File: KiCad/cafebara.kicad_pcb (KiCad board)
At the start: 4 copper layers, 50 x 26.8 mm, 31 parts, among them J1 Micro_SD_Card_Det2, J2 USB_C_Receptacle_USB2.0_14P, J3 PROG, J4 505278-1933, J5 I2C, Q1 NMOS, SW1 SW_Push, U3 ATtiny1616-M

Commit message: Minor misc updates
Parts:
- added TP6: HPD, TestPoint:TestPoint_Pad_D1.5mm, F.Cu at (87.5, 60.8)
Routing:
- net HPD: track 41.9 -> 56.7 mm, vias 2 -> 3
- net +3.3V: track 7.29 -> 0.00 mm

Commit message: Misc changes to cafebara, add temperature board
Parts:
- J4: value 505278-1933 -> Conn_01x19_MountingPin; moved to F.Cu
- moved J4 6.02 mm to (78.2, 70.5), turned to 0 degrees
- moved J1 0.50 mm to (93.8, 47.5)
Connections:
- J4 pad 1: TMDS2+ -> HPD
- J4 pad 11: GND -> TMDS0-
- J4 pad 12: TMDSClk- -> GND
- J4 pad 13: unconnected-(J4-Pad13) -> TMDS0+
- J4 pad 14: unconnected-(J4-Pad14) -> TMDS1-
- J4 pad 15: /HDMI_SCL -> GND
- J4 pad 16: /HDMI_SDA -> TMDS1+
- J4 pad 17: GND -> TMDS2-
- J4 pad 18: +5V -> GND
- J4 pad 19: HPD -> TMDS2+
- J4 pad 2: GND -> +5V
- J4 pad 3: TMDS2- -> GND
- J4 pad 4: TMDS1+ -> /HDMI_SDA
- J4 pad 5: GND -> /HDMI_SCL
- J4 pad 6: TMDS1- -> unconnected-(J4-Pin_6-Pad6)
- J4 pad 7: TMDS0+ -> unconnected-(J4-Pin_7-Pad7)
- J4 pad 8: GND -> TMDSClk-
- J4 pad 9: TMDS0- -> GND
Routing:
- net HPD: track 56.7 -> 62.4 mm
- net TMDSClk-: track 3.88 -> 3.14 mm, vias 1 -> 0
- net TMDS2+: track 3.79 -> 3.07 mm, vias 1 -> 0
- net TMDS0-: track 3.76 -> 3.13 mm, vias 1 -> 0
- net TMDS1-: track 3.64 -> 3.11 mm, vias 1 -> 0
- net SD_VCC: track 21.0 -> 21.5 mm
- net SD_DECT: track 14.4 -> 14.9 mm
- net SD_D3: track 14.0 -> 14.5 mm
- net SD_D2: track 14.3 -> 14.8 mm
- net SD_D1: track 21.4 -> 21.9 mm
- net SD_D0: track 17.3 -> 17.8 mm
- net SD_CMD: track 14.0 -> 14.5 mm
- net SD_CLK: track 14.2 -> 14.7 mm
- net TMDSClk+: track 3.61 -> 3.11 mm, vias 1 -> 0
- net TMDS0+: track 3.48 -> 3.06 mm, vias 1 -> 0
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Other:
- board size 50 x 26.8 mm -> 50 x 32 mm

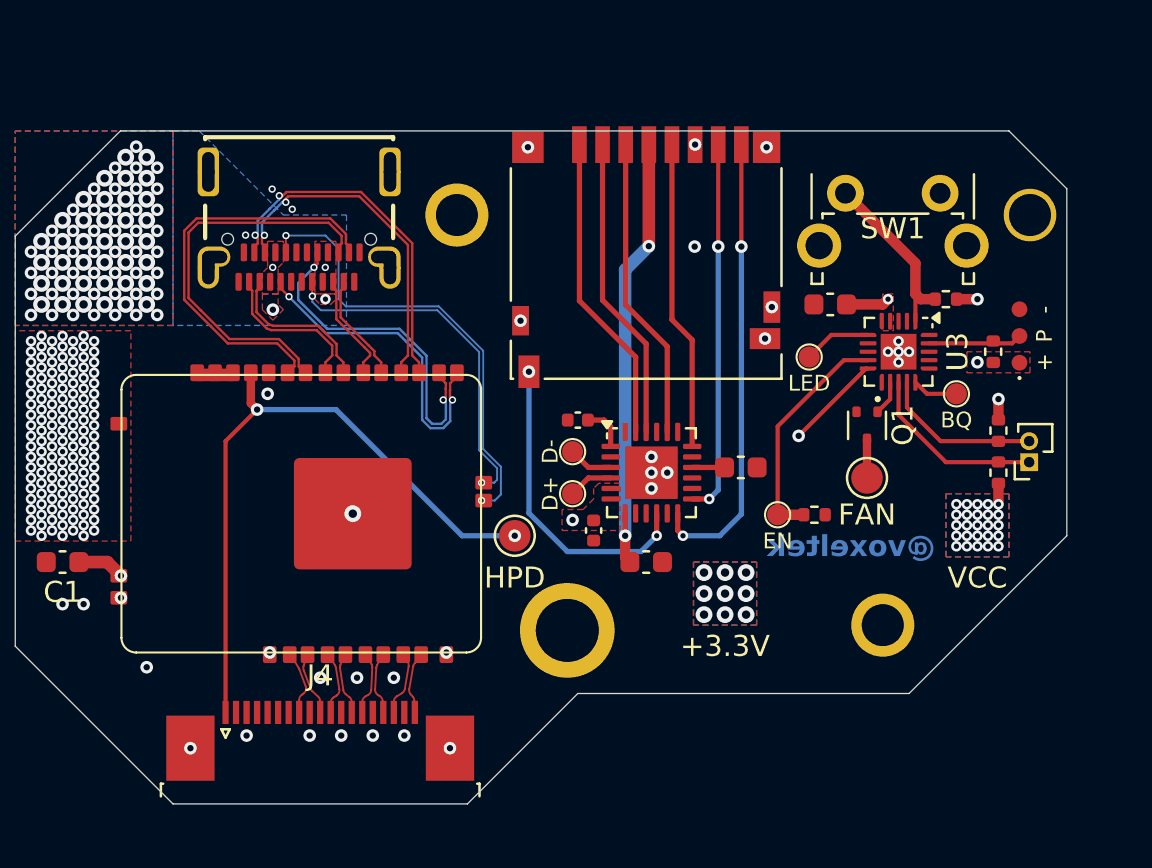
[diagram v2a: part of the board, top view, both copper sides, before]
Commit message: Add alert pin, EDID EEPROM, misc other changes
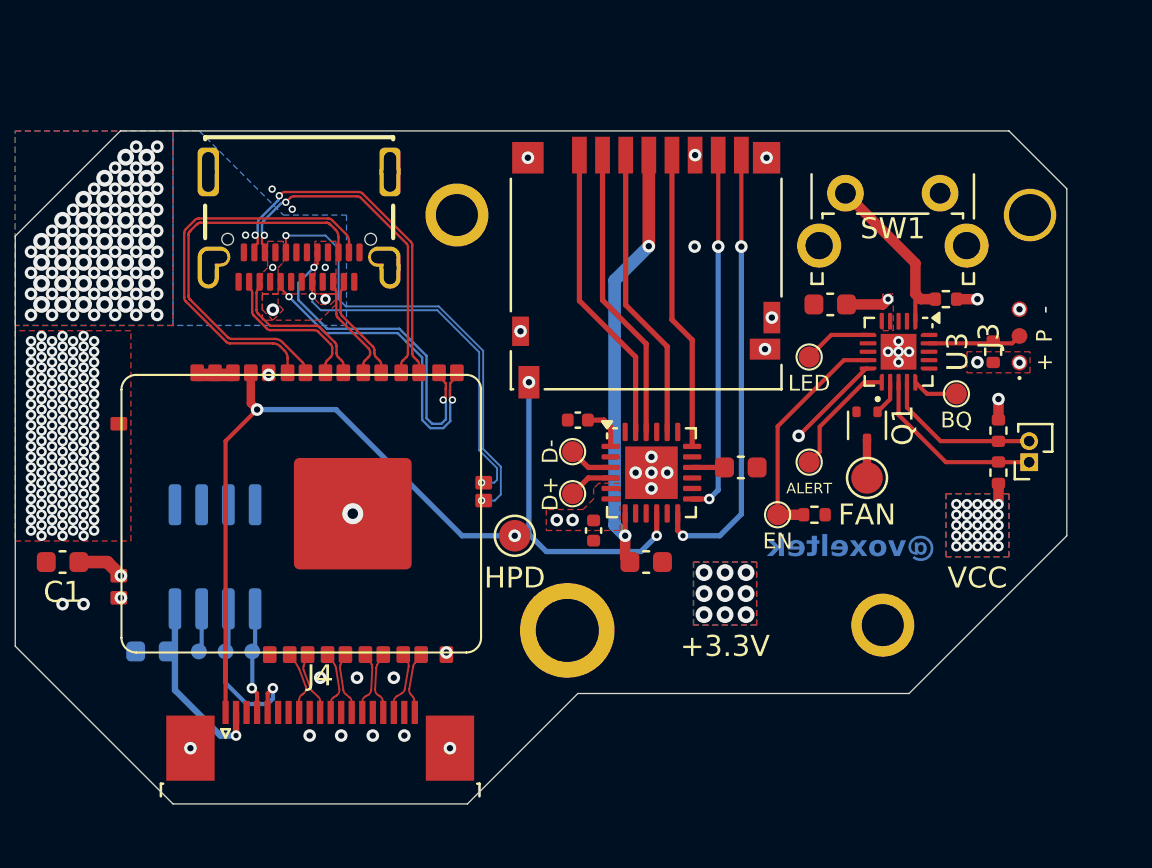
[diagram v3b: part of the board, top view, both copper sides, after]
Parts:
- added C7: 10uF, Capacitor_SMD:C_0603_1608Metric, B.Cu at (70.2, 66.2)
- added J6: EDID, cafebara:UPDI Pads, B.Cu at (73.8, 66.2)
- added TP7: ALERT, cafebara:TestPoint_Pad_D1.0mm_Small, F.Cu at (101.5, 57.2)
- added U4: M24C02-WMN, Package_SO:SOIC-8_3.9x4.9mm_P1.27mm, B.Cu at (73.2, 61.8)
- J3: footprint Stormbreaker:UPDI Pads -> cafebara:UPDI Pads
- moved J1 0.50 mm to (93.8, 48.0)
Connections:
- U3 pad 11: unconnected-(U3-PB3-Pad11) -> ~{ALERT}
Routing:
- net +5V: track 0.00 -> 8.77 mm, vias 0 -> 1
- net /HDMI_SCL: track 0.00 -> 8.10 mm, vias 0 -> 1
- net ~{ALERT}: track 0.00 -> 5.72 mm
- net /HDMI_SDA: track 0.00 -> 5.09 mm, vias 0 -> 1
- net /EEPROM_~{WC}: track 0.00 -> 2.08 mm
- net SD_D3: track 14.5 -> 14.0 mm
- net SD_D2: track 14.8 -> 14.3 mm
- net SD_D1: track 21.9 -> 21.4 mm
- net SD_D0: track 17.8 -> 17.3 mm
- net SD_CMD: track 14.5 -> 14.0 mm
- net SD_CLK: track 14.7 -> 14.2 mm
- net VCC: vias 29 -> 30
- net VBUS: vias 90 -> 91
- net GND: vias 173 -> 172
- net +3.3V: vias 10 -> 11

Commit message: Possibly planning to enlarge board...
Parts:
- removed the REF** at (112.0, 45.5)
- removed the REF** at (90.0, 65.2)
- removed the REF** at (105.0, 65.0)
- added H1: GND, TestPoint:TestPoint_Plated_Hole_D2.0mm, F.Cu at (105.0, 65.2)
- added H2: GND, TestPoint:TestPoint_Plated_Hole_D2.0mm, F.Cu at (112.0, 45.5)
- added H3: GND, TestPoint:TestPoint_Plated_Hole_D2.0mm, F.Cu at (90.0, 65.2)
- added H4: GND, TestPoint:TestPoint_Plated_Hole_D2.0mm, F.Cu at (66.5, 65.2)
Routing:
- net VBUS: vias 91 -> 60
- net GND: vias 172 -> 173
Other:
- outline, holes or cut-outs redrawn

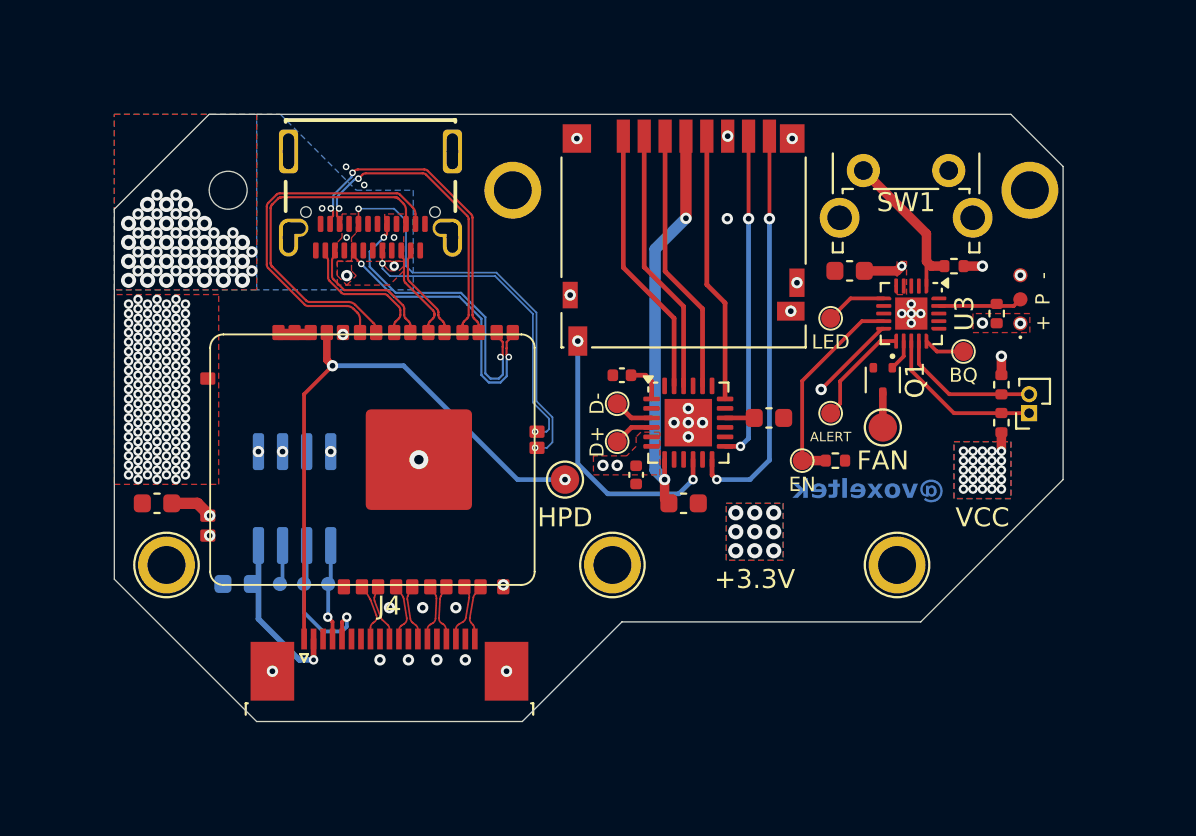
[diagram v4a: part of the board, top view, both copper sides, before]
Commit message: Expand board, add charge IC, other misc changes
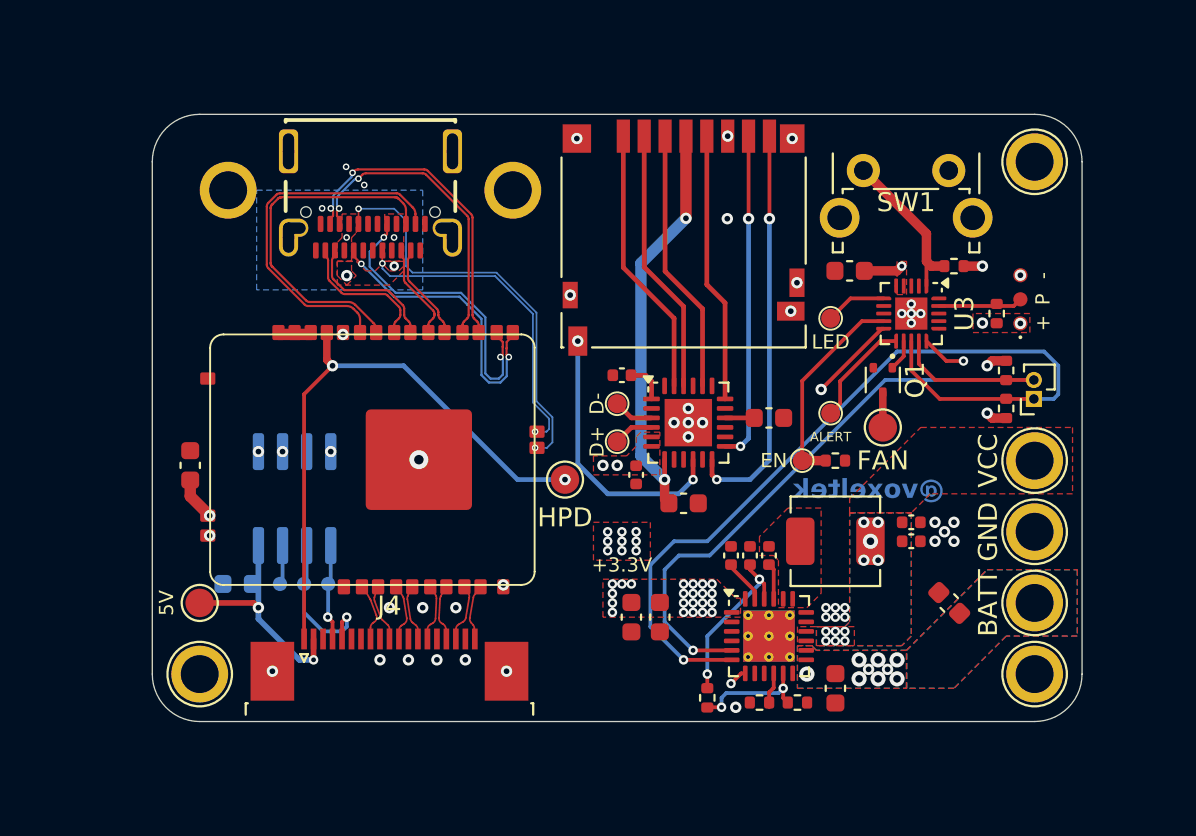
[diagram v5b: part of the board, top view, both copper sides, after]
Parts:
- added C10: 10uF, Capacitor_SMD:C_0402_1005Metric, F.Cu at (105.8, 63.0)
- added C11: 10uF, Capacitor_SMD:C_0402_1005Metric, F.Cu at (105.8, 64.0)
- added C12: 47nF, Capacitor_SMD:C_0402_1005Metric, F.Cu at (98.2, 64.8)
- added C13: 10uF, Capacitor_SMD:C_0603_1608Metric, F.Cu at (107.8, 67.2)
- added C14: 4.7uF, Capacitor_SMD:C_0402_1005Metric, F.Cu at (97.2, 64.8)
- added C15: 10uF, Capacitor_SMD:C_0603_1608Metric, F.Cu at (92.5, 68.0)
- added C16: 10uF, Capacitor_SMD:C_0603_1608Metric, F.Cu at (101.8, 71.8)
- added C8: 22uF, Capacitor_SMD:C_0402_1005Metric, F.Cu at (96.2, 64.8)
- added C9: 10uF, Capacitor_SMD:C_0603_1608Metric, F.Cu at (91.0, 68.0)
- added L1: 3.3uH, Inductor_SMD:L_APV_APH0420, F.Cu at (101.8, 64.0)
- added R6: 260, Resistor_SMD:R_0402_1005Metric, F.Cu at (97.8, 72.5)
- added R7: 5.23k, Resistor_SMD:R_0402_1005Metric, F.Cu at (95.0, 72.2)
- added R8: 30.1k, Resistor_SMD:R_0402_1005Metric, F.Cu at (99.8, 72.5)
- added TP11: 5V, TestPoint:TestPoint_Pad_D1.5mm, F.Cu at (68.2, 67.2)
- added TP8: VCC, TestPoint:TestPoint_Plated_Hole_D2.0mm, F.Cu at (112.2, 59.8)
- added TP9: GND, TestPoint:TestPoint_Plated_Hole_D2.0mm, F.Cu at (112.2, 63.5)
- added U5: BQ25895RTW, Package_DFN_QFN:Texas_RTW_WQFN-24-1EP_4x4mm_P0.5mm_EP2.7x2.7mm_ThermalVias, F.Cu at (98.2, 69.0)
- TP5: value BQ -> BATT; footprint cafebara:TestPoint_Pad_D1.0mm_Small -> TestPoint:TestPoint_Plated_Hole_D2.0mm
- moved H4 50.4 mm to (112.2, 44.0)
- moved H2 42.2 mm to (69.8, 45.5)
- moved H1 37.2 mm to (68.2, 71.0)
- moved H3 23.0 mm to (112.2, 71.0)
- moved TP5 13.8 mm to (112.2, 67.2), turned to -90 degrees
- moved C1 2.66 mm to (67.8, 60.0), turned to 90 degrees
- moved J5 0.79 mm to (112.2, 56.5)
- moved R1 0.79 mm to (110.8, 55.0)
- moved R2 0.79 mm to (110.8, 57.0)
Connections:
- TP5 pad 1: /BQ_STAT -> /BATT
- U1 pad 27: +3.3V_LDO -> GND
- U3 pad 15: /BQ_STAT -> ~{INT}
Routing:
- net SDA: track 8.69 -> 46.3 mm, vias 0 -> 1
- net SCL: track 7.67 -> 38.1 mm, vias 0 -> 1
- net ~{INT}: track 0.00 -> 26.0 mm, vias 0 -> 2
- net Net-(U5-REGN): track 0.00 -> 9.00 mm, vias 0 -> 2
- net Net-(U5-TS): track 0.00 -> 6.33 mm, vias 0 -> 2
- net VBUS: track 15.5 -> 20.1 mm, vias 60 -> 27
- net +5V: track 8.77 -> 12.0 mm, vias 1 -> 2
- net Net-(U5-PMID): track 0.00 -> 2.33 mm
- net /BQ_STAT: track 2.18 -> 0.00 mm
- net Net-(U5-BTST): track 0.00 -> 1.91 mm
- net Net-(U5-ILIM): track 0.00 -> 1.88 mm
- net SD_VCC: track 21.4 -> 22.0 mm
- net VCC: track 5.05 -> 5.28 mm, vias 30 -> 17
- net GND: vias 173 -> 49
- net /BATT: vias 0 -> 9
- added copper zone on B.Cu, net /BATT
- added copper zone on F.Cu, net /BATT
- added copper zone on In2.Cu, net /BATT
- added copper zone on F.Cu, net Net-(C12-Pad1)
- removed copper zone on B.Cu, net +3.3V
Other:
- board size 50 x 32 mm -> 49 x 32 mm
- board text removed: "VCC"

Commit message: Misc minor board adjustments
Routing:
- net +3.3V_LDO: track 1.70 -> 0.85 mm

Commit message: Misc
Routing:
- net ~{INT}: track 26.0 -> 27.2 mm
